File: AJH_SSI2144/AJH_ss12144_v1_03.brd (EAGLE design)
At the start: 19 x 106.8 mm, 57 parts, among them IC1 LM4040 5.0V, IC2 TL074D, IC3 TL072D, J100 PJ301_THONKICONN6, J101 PJ301_THONKICONN6, J102 PJ301_THONKICONN6, J103 PJ301_THONKICONN6, U1 BCM847BS

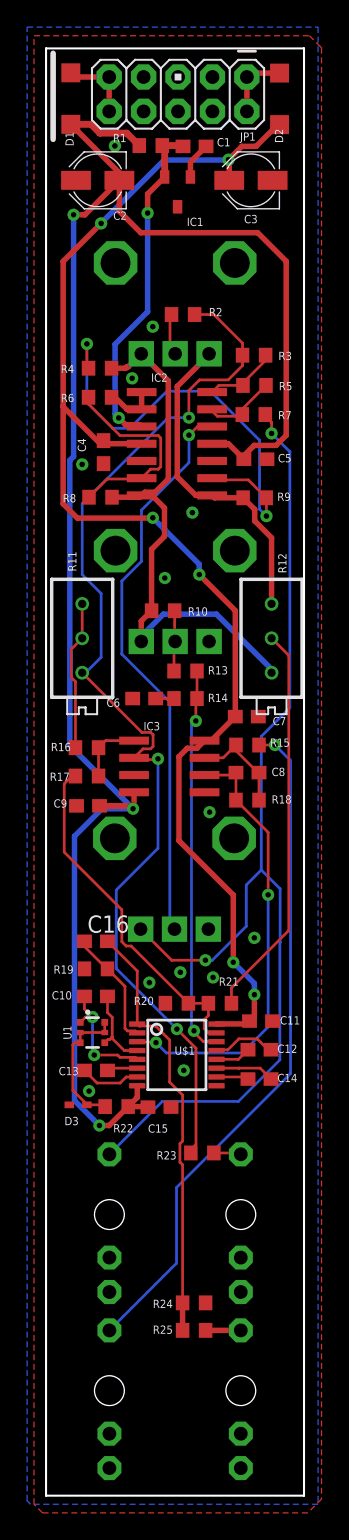
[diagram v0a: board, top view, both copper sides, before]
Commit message: Add through hole tempco to ssi2144
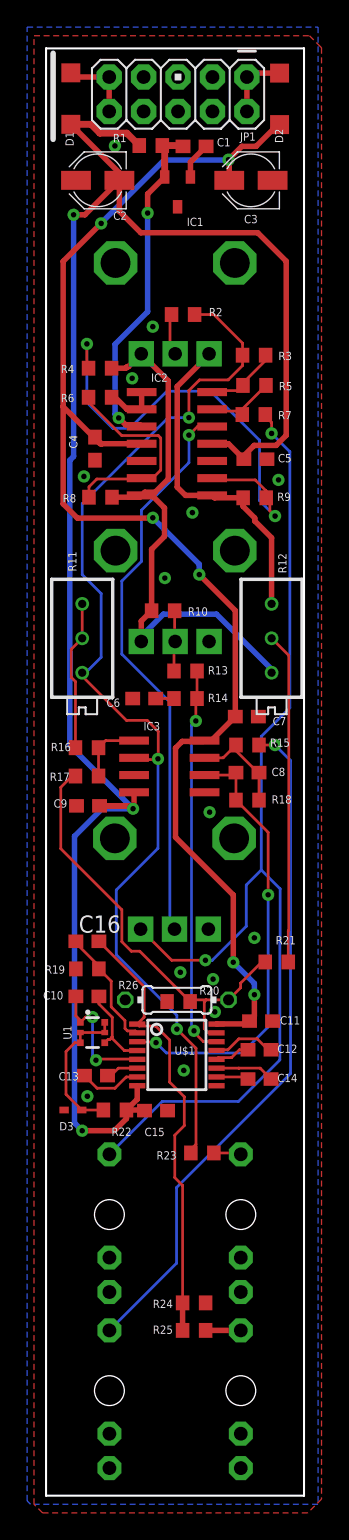
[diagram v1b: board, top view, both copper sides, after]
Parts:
- added R26: DNP, rcl:0204/7
- moved R21 5.18 mm to (17.0, 39.4)
- moved C4 0.68 mm to (3.61, 77.2)
- moved C10 0.63 mm to (3.05, 36.8)
- moved C16 0.63 mm to (3.05, 40.9)
- moved R19 0.63 mm to (3.05, 38.9)
- moved D3 0.54 mm to (2.03, 28.4)
- moved C13 0.38 mm to (3.68, 31.0)
- moved C15 0.36 mm to (8.11, 28.4)
- moved R22 0.28 mm to (5.08, 28.4)
- moved R20 0.18 mm to (9.78, 36.4)
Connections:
- net FREQ_IN: now also R26.2
- net GND: now also R26.1
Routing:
- net FREQ_IN: track 25.8 -> 31.7 mm
- net N$27: track 29.2 -> 24.4 mm
- net -12V: track 136.7 -> 138.3 mm
- net N$28: track 31.9 -> 33.0 mm
- net 12V: track 100.9 -> 102.0 mm
- net N$14: track 10.2 -> 11.0 mm
- net N$13: track 34.1 -> 34.9 mm
- net N$15: track 15.2 -> 15.8 mm
- net GND: vias 13 -> 14
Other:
- board text added: "ssi2144 lpf v1.03, copyright forestcaver 2020"
- board text removed: "ssi2144 lpf v1.02, copyright forestcaver 2020"

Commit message: Typo on ssi2144 schematic comments
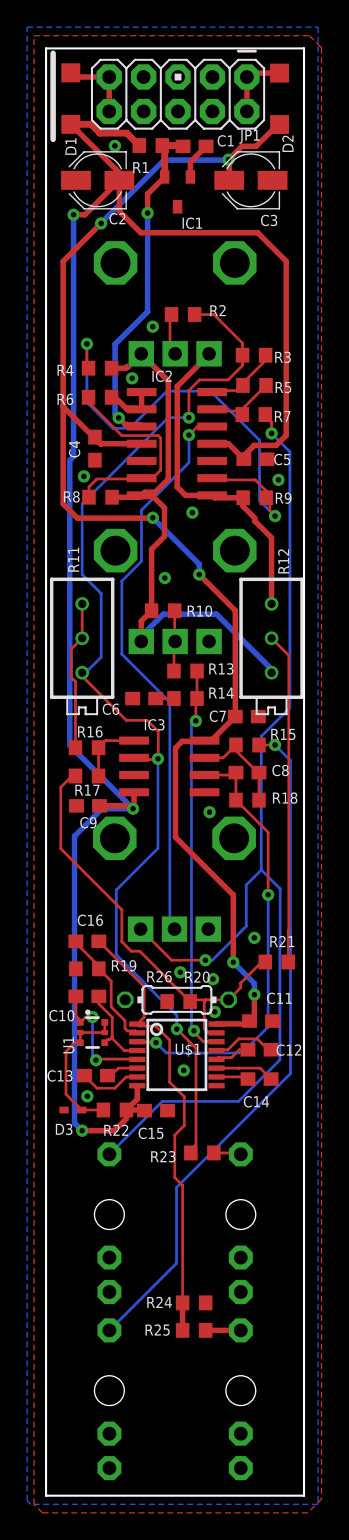
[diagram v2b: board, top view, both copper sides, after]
